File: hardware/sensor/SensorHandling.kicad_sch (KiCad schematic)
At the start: 3 parts, among them Q1 NMOS, U1 Opamp

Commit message: commit to save work from misbehaving laptop
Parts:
- removed U1: Opamp, symbol Device:Opamp_Dual
- added Q? (x2): BC847BDW1, Package_TO_SOT_SMD:SOT-363_SC-70-6, symbol Transistor_BJT:BC847BDW1
- added R?: 4k7, symbol Device:R
- added U? (x2): LTC2064, Package_SO:MSOP-8_3x3mm_P0.65mm, symbol sensorModules:LTC2064IMS8
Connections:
- net GND: now also R?.2, U?.11 (V-), U?.4 (V-)
- net Out: now also U?.9
- net V_{DD}: now also U?.10 (V+)
- net V_{ref}: now also Q?.2 (B1), U?.7 (+)
- net Current/In: no longer names the net of C1.2, Q1.3 (S)
- net Current/In: now also Q?.6 (C1), U?.8 (-)
- new net: Q?.1 (E1), R?.1
- new net shutdown: U?.6 (~{SHDN})
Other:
- removed sheet Current
- moved on the sheet: C1

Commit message: Fix incorrect upstream
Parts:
- added C402: 100n, Capacitor_SMD:C_0805_2012Metric_Pad1.18x1.45mm_HandSolder, symbol Device:C
- added J401: U_{SS}, testpoint_519x:Testpoint_519xTR, symbol Connector:Conn_01x01_Pin
- added J402: U_{DD}, testpoint_519x:Testpoint_519xTR, symbol Connector:Conn_01x01_Pin
- added J405: Out, testpoint_519x:Testpoint_519xTR, symbol Connector:Conn_01x01_Pin
- added J502 (x2): GND, testpoint_519x:Testpoint_519xTR, symbol Connector:Conn_01x01_Pin
- C401: renamed from C1; value C -> TBD; footprint (none) -> Capacitor_SMD:C_0805_2012Metric_Pad1.18x1.45mm_HandSolder
- Q402: renamed from Q1; footprint (none) -> Connector_PinHeader_2.54mm:PinHeader_1x03_P2.54mm_Horizontal
- R401: renamed from R?; footprint (none) -> Resistor_SMD:R_0805_2012Metric_Pad1.20x1.40mm_HandSolder
- gave numbers to parts that had none: 1
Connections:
- net shutdown is gone; now on an unnamed net: U?.6 (-)
- net GND: now also C402.2, J502.1 (Pin_1), J502.1 (Pin_1); no longer U?.11 (V-)
- net Out: now also Q402.3 (G), U?.7, J405.1 (Pin_1); no longer Q402.2 (G), U?.9
- net V_{DD}: now also U?.8 (V+), C402.1, J402.1 (Pin_1); no longer U?.10 (V+)
- net V_{ref}: now also U?.5 (+); no longer U?.7 (+)
- net at C401.2, Q401.6 (C1): now also Q402.2 (S), J401.1 (Pin_1); no longer Q402.3 (S), U?.8 (-)
- no-connect marks 0 -> 3
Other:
- moved on the sheet: C401, Q401A, Q401B, R401

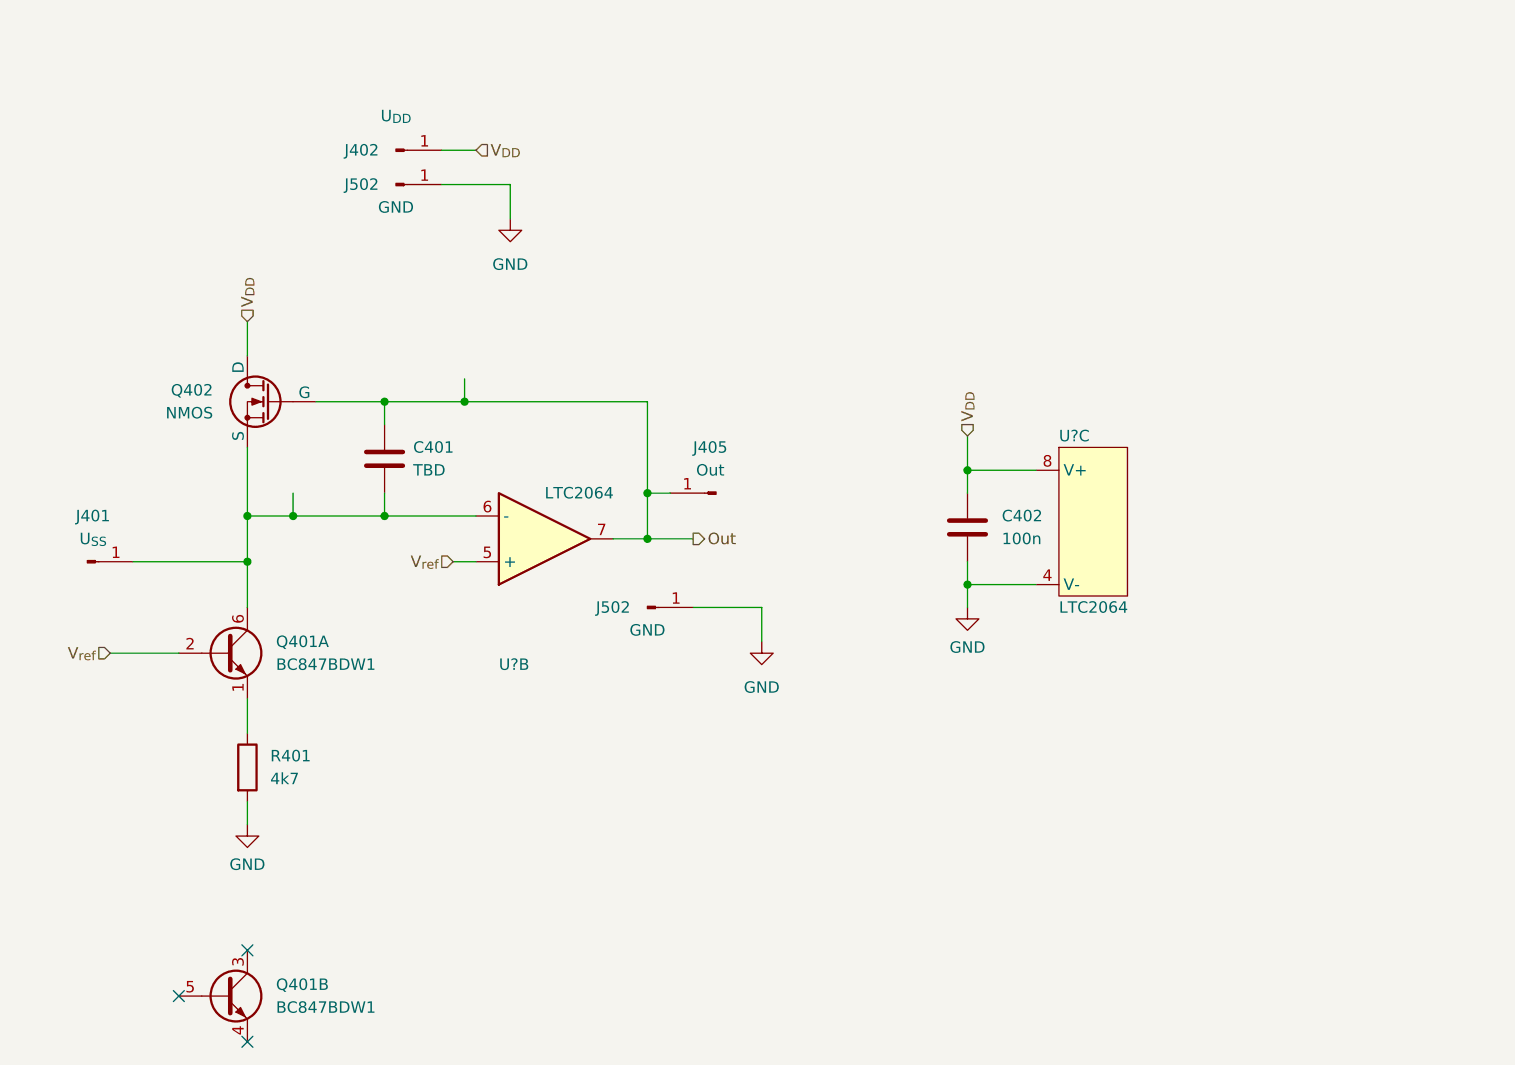
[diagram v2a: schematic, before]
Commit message: Finished initial pcb routing
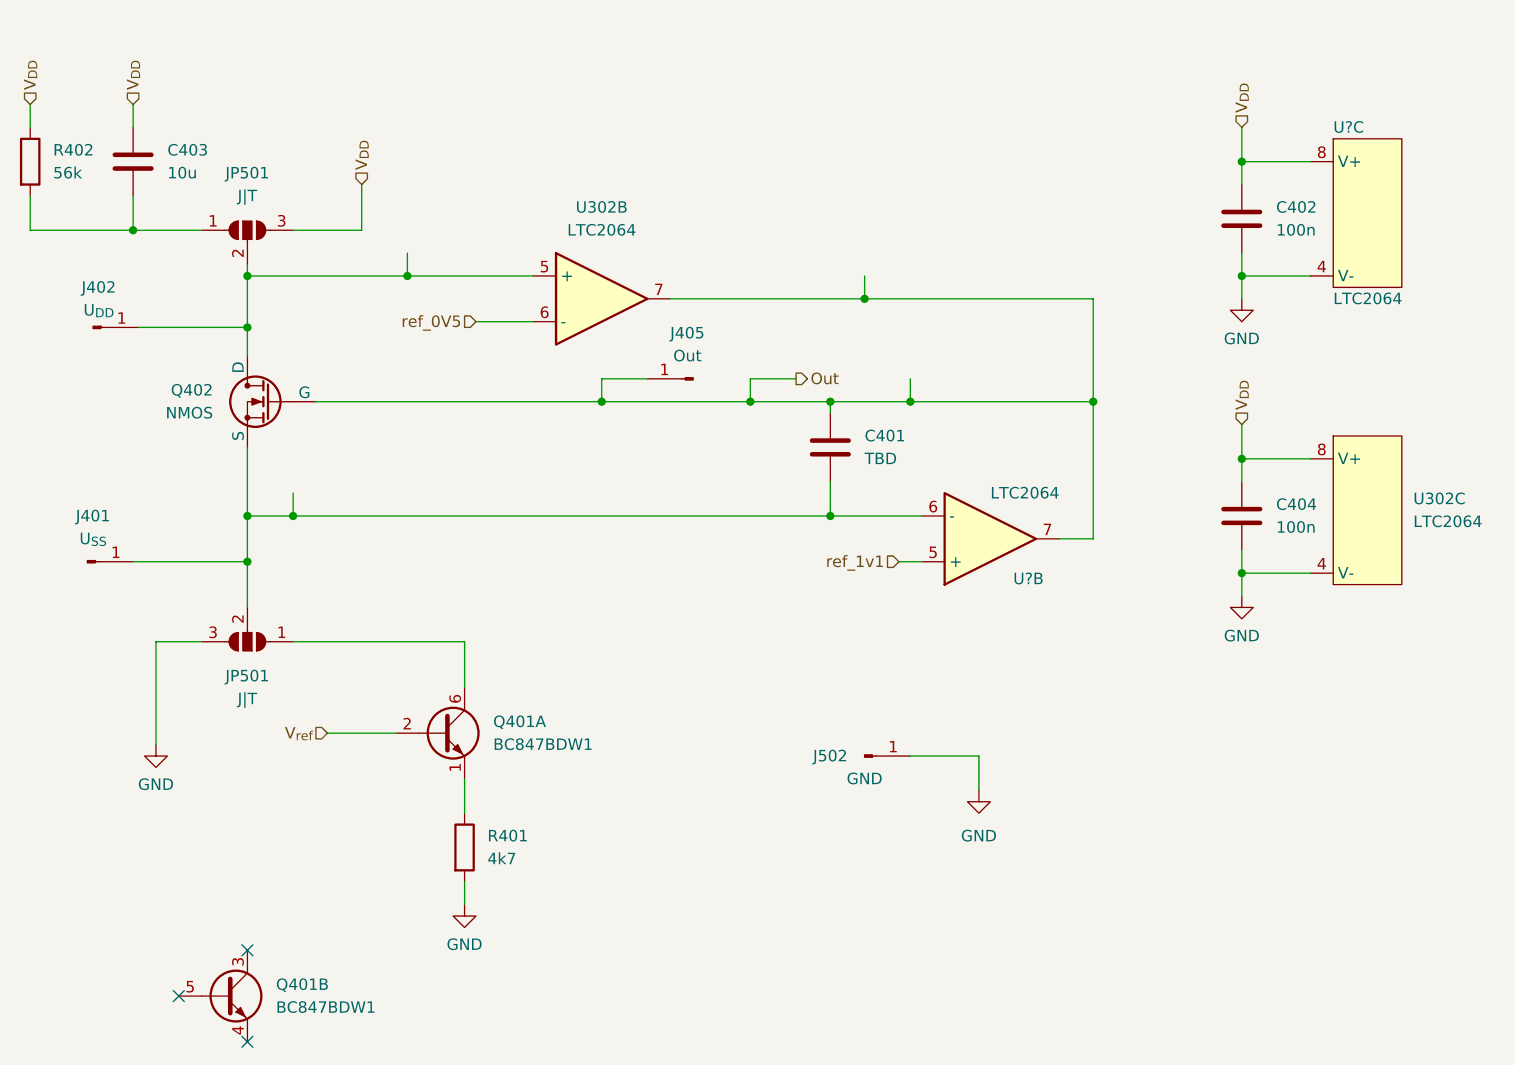
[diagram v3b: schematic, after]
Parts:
- removed J502: GND, testpoint_519x:Testpoint_519xTR, symbol Connector:Conn_01x01_Pin
- added C403: 10u, Capacitor_SMD:C_0805_2012Metric_Pad1.18x1.45mm_HandSolder, symbol Device:C
- added C404: 100n, Capacitor_SMD:C_0805_2012Metric_Pad1.18x1.45mm_HandSolder, symbol Device:C
- added JP501 (x2): J|T, Jumper:SolderJumper-3_P1.3mm_Open_RoundedPad1.0x1.5mm, symbol Jumper:SolderJumper_3_Open
- added R402: 56k, Resistor_SMD:R_0805_2012Metric_Pad1.20x1.40mm_HandSolder, symbol Device:R
- added U302: LTC2064, Package_SO:MSOP-8_3x3mm_P0.65mm, symbol sensorModules:LTC2064IMS8
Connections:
- net GND: now also C404.2, JP501.3 (B), U302.4 (V-)
- net Out: now also U302.7
- net V_{DD}: now also C403.1, C404.1, JP501.3 (B), R402.1, U302.8 (V+); no longer J402.1 (Pin_1), Q402.1 (D)
- net V_{ref}: no longer U?.5 (+)
- net at C401.2, J401.1 (Pin_1), Q402.2 (S)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: now also JP501.2 (C); no longer Q401.6 (C1)
- new net: J402.1 (Pin_1), JP501.2 (C), Q402.1 (D), U302.5 (+)
- new net: C403.2, JP501.1 (A), R402.2
- new net: JP501.1 (A), Q401.6 (C1)
- new net ref_0V5: U302.6 (-)
- new net ref_1v1: U?.5 (+)
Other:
- moved on the sheet: C401, C402, J405, J502, Q401A, R401, U?B, U?C

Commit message: Add bom and final version of rev 1.0
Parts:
- Q401: Digikey (none) -> BC847BDW1T3GOSCT-ND; Farnell (none) -> 2533306
- U302, U? (x2): Digikey (none) -> 505-LTC2064IMS8#PBF-ND
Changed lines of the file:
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@@
+      (effects (font (size 1.27 1.27)) hide)
+    )
+    (property "Digikey" "" (at 171.45 31.75 0)
       (effects (font (size 1.27 1.27)) hide)
     )
@@
     )
     (property "Farnell" "4021217" (at 185.42 31.75 0)
+      (effects (font (size 1.27 1.27)) hide)
+    )
+    (property "Digikey" "505-LTC2064IMS8#PBF-ND" (at 185.42 31.75 0)
       (effects (font (size 1.27 1.27)) hide)
     )
@@
       (effects (font (size 1.27 1.27)) hide)
     )
+    (property "Digikey" "" (at 171.45 64.77 0)
+      (effects (font (size 1.27 1.27)) hide)
+    )
     (pin "1")
     (pin "2")
@@
       (effects (font (size 1.27 1.27)) hide)
     )
+    (property "Digikey" "" (at 63.5 52.07 0)
+      (effects (font (size 1.27 1.27)) hide)
+    )
     (pin "1")
     (pin "3")
@@
     )
     (property "Datasheet" "~" (at 129.54 91.44 0)
+      (effects (font (size 1.27 1.27)) hide)
+    )
+    (property "Digikey" "" (at 129.54 91.44 0)
       (effects (font (size 1.27 1.27)) hide)
     )
@@
     )
     (property "Farnell" "4021217" (at 99.06 40.64 0)
+      (effects (font (size 1.27 1.27)) hide)
+    )
+    (property "Digikey" "505-LTC2064IMS8#PBF-ND" (at 99.06 40.64 0)
       (effects (font (size 1.27 1.27)) hide)
     )
@@
       (effects (font (size 1.27 1.27)) hide)
     )
+    (property "Digikey" "505-LTC2064IMS8#PBF-ND" (at 185.42 64.77 0)
+      (effects (font (size 1.27 1.27)) hide)
+    )
     (pin "7")
     (pin "1")
@@
       (effects (font (size 1.27 1.27)) hide)
     )
+    (property "Digikey" "BC847BDW1T3GOSCT-ND" (at 58.42 118.11 0)
+      (effects (font (size 1.27 1.27)) hide)
+    )
+    (property "Farnell" "2533306" (at 58.42 118.11 0)
+      (effects (font (size 1.27 1.27)) hide)
+    )
     (pin "6")
     (pin "5")
@@
       (effects (font (size 1.27 1.27)) hide)
     )
+    (property "Digikey" "" (at 110.49 49.53 0)
+      (effects (font (size 1.27 1.27)) hide)
+    )
     (pin "1")
     (instances
@@
       (effects (font (size 1.27 1.27)) hide)
     )
+    (property "Digikey" "" (at 43.815 43.815 0)
+      (effects (font (size 1.27 1.27)) hide)
+    )
     (pin "1")
     (instances
@@
     )
     (property "Datasheet" "~" (at 60.96 33.02 0)
+      (effects (font (size 1.27 1.27)) hide)
+    )
+    (property "Digikey" "~" (at 60.96 33.02 0)
+      (effects (font (size 1.27 1.27)) hide)
+    )
+    (property "Farnell" "~" (at 60.96 33.02 0)
       (effects (font (size 1.27 1.27)) hide)
     )
@@
       (effects (font (size 1.27 1.27)) hide)
     )
+    (property "Digikey" "" (at 85.09 101.6 0)
+      (effects (font (size 1.27 1.27)) hide)
+    )
     (pin "2")
     (pin "1")
@@
     )
     (property "Farnell" "4021217" (at 142.24 67.31 0)
+      (effects (font (size 1.27 1.27)) hide)
+    )
+    (property "Digikey" "505-LTC2064IMS8#PBF-ND" (at 142.24 67.31 0)
       (effects (font (size 1.27 1.27)) hide)
     )
@@
       (effects (font (size 1.27 1.27)) hide)
     )
+    (property "Digikey" "~" (at 60.96 78.74 0)
+      (effects (font (size 1.27 1.27)) hide)
+    )
+    (property "Farnell" "~" (at 60.96 78.74 0)
+      (effects (font (size 1.27 1.27)) hide)
+    )
     (pin "3")
     (pin "2")
@@
       (effects (font (size 1.27 1.27)) hide)
     )
+    (property "Digikey" "BC847BDW1T3GOSCT-ND" (at 82.55 88.9 0)
+      (effects (font (size 1.27 1.27)) hide)
+    )
+    (property "Farnell" "2533306" (at 82.55 88.9 0)
+      (effects (font (size 1.27 1.27)) hide)
+    )
     (pin "6")
     (pin "5")
@@
       (effects (font (size 1.27 1.27)) hide)
     )
+    (property "Digikey" "" (at 125.73 57.15 0)
+      (effects (font (size 1.27 1.27)) hide)
+    )
     (pin "2")
     (pin "1")
@@
       (effects (font (size 1.27 1.27)) hide)
     )
+    (property "Digikey" "" (at 48.26 25.4 0)
+      (effects (font (size 1.27 1.27)) hide)
+    )
     (pin "1")
     (pin "2")
@@
       (effects (font (size 1.27 1.27)) hide)
     )
+    (property "Digikey" "" (at 43.18 69.85 0)
+      (effects (font (size 1.27 1.27)) hide)
+    )
     (pin "1")
     (instances
@@
       (effects (font (size 1.27 1.27)) hide)
     )
+    (property "Digikey" "" (at 36.83 25.4 0)
+      (effects (font (size 1.27 1.27)) hide)
+    )
